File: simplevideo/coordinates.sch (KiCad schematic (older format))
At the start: 3 parts, among them U1 4040, U4 4040, U5 4040

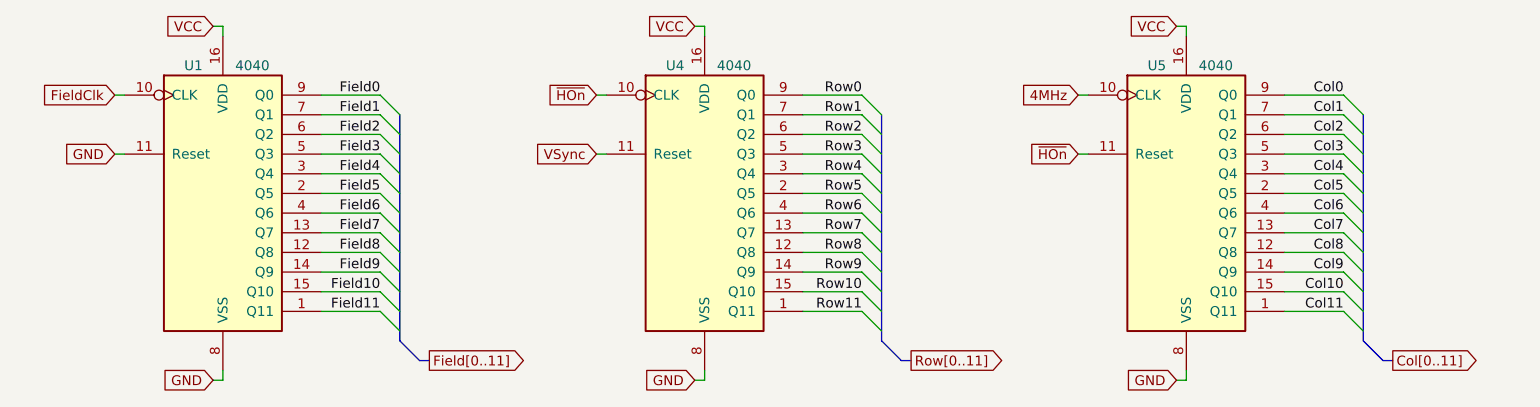
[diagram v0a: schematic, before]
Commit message: Include 6502, ROM, etc in circuit, all laid out together
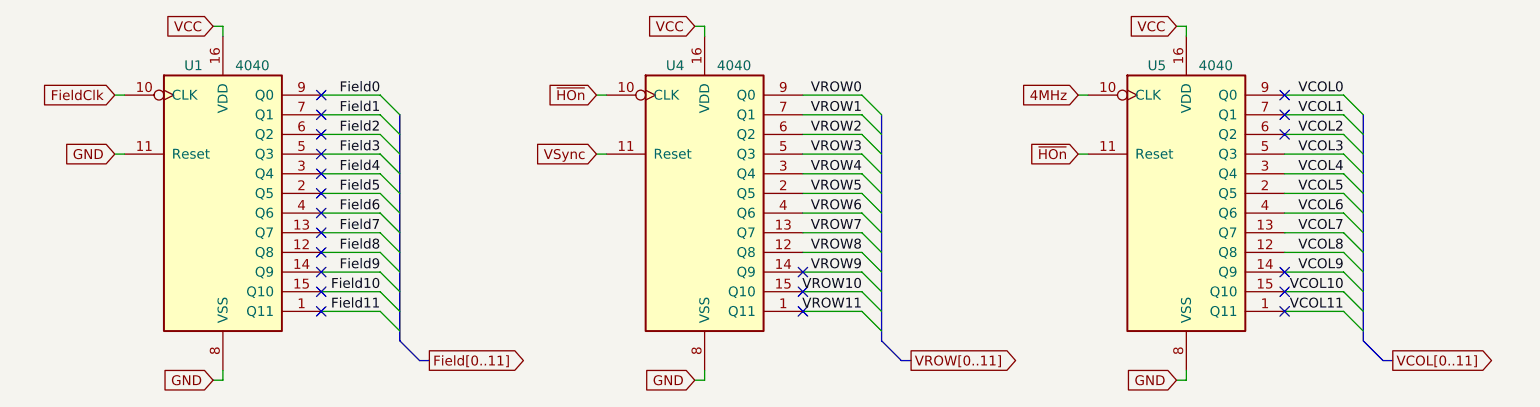
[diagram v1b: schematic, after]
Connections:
- net Col0 renamed VCOL0
- net Col1 renamed VCOL1
- net Col10 renamed VCOL10
- net Col11 renamed VCOL11
- net Col2 renamed VCOL2
- net Col3 renamed VCOL3
- net Col4 renamed VCOL4
- net Col5 renamed VCOL5
- net Col6 renamed VCOL6
- net Col7 renamed VCOL7
- net Col8 renamed VCOL8
- net Col9 renamed VCOL9
- net Row0 renamed VROW0
- net Row1 renamed VROW1
- net Row10 renamed VROW10
- net Row11 renamed VROW11
- net Row2 renamed VROW2
- net Row3 renamed VROW3
- net Row4 renamed VROW4
- net Row5 renamed VROW5
- net Row6 renamed VROW6
- net Row7 renamed VROW7
- net Row8 renamed VROW8
- net Row9 renamed VROW9
- no-connect marks 0 -> 21
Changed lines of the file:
@@
 $Descr A4 11693 8268
 encoding utf-8
-Sheet 5 5
+Sheet 5 7
 Title ""
 Date ""
@@
 	6800 4400 6850 4400
 Text GLabel 6850 4400 2    50   Output ~ 0
-Row[0..11]
+VROW[0..11]
 $Comp
 L 4xxx:4040 U5
@@
 	9250 4400 9300 4400
 Text GLabel 9300 4400 2    50   Output ~ 0
-Col[0..11]
+VCOL[0..11]
 Text Label 4150 3050 2    50   ~ 0
 Field0
@@
 Text Label 4150 4150 2    50   ~ 0
 Field11
-Text Label 6600 3050 2    50   ~ 0
-Row0
-Text Label 6600 3150 2    50   ~ 0
-Row1
-Text Label 6600 3250 2    50   ~ 0
-Row2
-Text Label 6600 3350 2    50   ~ 0
-Row3
-Text Label 6600 3450 2    50   ~ 0
-Row4
-Text Label 6600 3550 2    50   ~ 0
-Row5
-Text Label 6600 3650 2    50   ~ 0
-Row6
-Text Label 6600 3750 2    50   ~ 0
-Row7
-Text Label 6600 3850 2    50   ~ 0
-Row8
-Text Label 6600 3950 2    50   ~ 0
-Row9
-Text Label 6600 4050 2    50   ~ 0
-Row10
-Text Label 6600 4150 2    50   ~ 0
-Row11
-Text Label 9050 3050 2    50   ~ 0
-Col0
-Text Label 9050 3150 2    50   ~ 0
-Col1
-Text Label 9050 3250 2    50   ~ 0
-Col2
-Text Label 9050 3350 2    50   ~ 0
-Col3
-Text Label 9050 3450 2    50   ~ 0
-Col4
-Text Label 9050 3550 2    50   ~ 0
-Col5
-Text Label 9050 3650 2    50   ~ 0
-Col6
-Text Label 9050 3750 2    50   ~ 0
-Col7
-Text Label 9050 3850 2    50   ~ 0
-Col8
-Text Label 9050 3950 2    50   ~ 0
-Col9
-Text Label 9050 4050 2    50   ~ 0
-Col10
-Text Label 9050 4150 2    50   ~ 0
-Col11
 Text GLabel 7700 3050 0    50   Input ~ 0
 4MHz
 Text GLabel 7700 3350 0    50   Input ~ 0
 ~HOn
+Text Label 9050 3050 2    50   ~ 0
+VCOL0
+Text Label 9050 3150 2    50   ~ 0
+VCOL1
+Text Label 9050 3250 2    50   ~ 0
+VCOL2
+Text Label 9050 3350 2    50   ~ 0
+VCOL3
+Text Label 9050 3450 2    50   ~ 0
+VCOL4
+Text Label 9050 3550 2    50   ~ 0
+VCOL5
+Text Label 9050 3650 2    50   ~ 0
+VCOL6
+Text Label 9050 3750 2    50   ~ 0
+VCOL7
+Text Label 9050 3850 2    50   ~ 0
+VCOL8
+Text Label 9050 3950 2    50   ~ 0
+VCOL9
+Text Label 9050 4050 2    50   ~ 0
+VCOL10
+Text Label 9050 4150 2    50   ~ 0
+VCOL11
+Text Label 6600 3050 2    50   ~ 0
+VROW0
+Text Label 6600 3150 2    50   ~ 0
+VROW1
+Text Label 6600 3250 2    50   ~ 0
+VROW2
+Text Label 6600 3350 2    50   ~ 0
+VROW3
+Text Label 6600 3450 2    50   ~ 0
+VROW4
+Text Label 6600 3550 2    50   ~ 0
+VROW5
+Text Label 6600 3650 2    50   ~ 0
+VROW6
+Text Label 6600 3750 2    50   ~ 0
+VROW7
+Text Label 6600 3850 2    50   ~ 0
+VROW8
+Text Label 6600 3950 2    50   ~ 0
+VROW9
+Text Label 6600 4050 2    50   ~ 0
+VROW10
+Text Label 6600 4150 2    50   ~ 0
+VROW11
+NoConn ~ 8750 3950
+NoConn ~ 8750 4050
+NoConn ~ 8750 4150
+NoConn ~ 6300 3950
+NoConn ~ 6300 4050
+NoConn ~ 6300 4150
+NoConn ~ 3850 3050
+NoConn ~ 3850 3150
+NoConn ~ 3850 3250
+NoConn ~ 3850 3350
+NoConn ~ 3850 3450
+NoConn ~ 3850 3550
+NoConn ~ 3850 3650
+NoConn ~ 3850 3750
+NoConn ~ 3850 3850
+NoConn ~ 3850 4050
+NoConn ~ 3850 3950
+NoConn ~ 3850 4150
+NoConn ~ 8750 3150
+NoConn ~ 8750 3050
+NoConn ~ 8750 3250
 Wire Bus Line
 	4250 3150 4250 4300

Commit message: New address decoding scheme and complete breadboard layout, should be ready to build
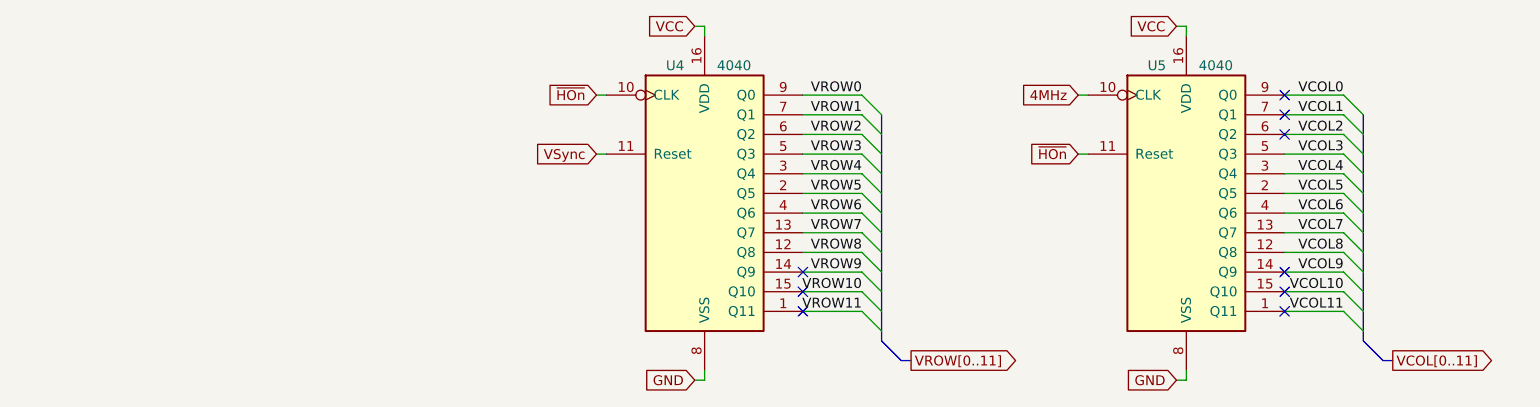
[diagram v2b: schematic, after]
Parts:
- removed U1: 4040, Package_DIP:DIP-16_W7.62mm, symbol 4xxx:4040
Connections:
- no-connect marks 21 -> 9
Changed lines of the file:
@@
 $EndDescr
-$Comp
-L 4xxx:4040 U1
-U 1 1 5EE32031
-P 3350 3550
-F 0 "U1" H 3200 4200 50  0000 C CNN
-F 1 "4040" H 3500 4200 50  0000 C CNN
-F 2 "Package_DIP:DIP-16_W7.62mm" H 3350 3550 50  0001 C CNN
-F 3 "http://www.intersil.com/content/dam/Intersil/documents/cd40/cd4020bms-24bms-40bms.pdf" H 3350 3550 50  0001 C CNN
-	1    3350 3550
-	1    0    0    -1
-$EndComp
-Text GLabel 2800 3050 0    50   Input ~ 0
-FieldClk
-Wire Wire Line
-	2800 3050 2850 3050
-Wire Wire Line
-	2850 3350 2800 3350
-Text GLabel 2800 3350 0    50   Input ~ 0
-GND
-Text GLabel 3300 4500 0    50   Input ~ 0
-GND
-Wire Wire Line
-	3300 4500 3350 4500
-Wire Wire Line
-	3350 4500 3350 4450
-Text GLabel 3300 2700 0    50   Input ~ 0
-VCC
-Wire Wire Line
-	3300 2700 3350 2700
-Wire Wire Line
-	3350 2700 3350 2750
-Wire Wire Line
-	3850 3050 4150 3050
-Wire Wire Line
-	3850 3150 4150 3150
-Wire Wire Line
-	3850 3250 4150 3250
-Wire Wire Line
-	3850 3350 4150 3350
-Wire Wire Line
-	3850 3450 4150 3450
-Wire Wire Line
-	3850 3550 4150 3550
-Wire Wire Line
-	3850 3650 4150 3650
-Wire Wire Line
-	3850 3750 4150 3750
-Wire Wire Line
-	3850 3850 4150 3850
-Wire Wire Line
-	3850 3950 4150 3950
-Wire Wire Line
-	3850 4050 4150 4050
-Wire Wire Line
-	3850 4150 4150 4150
-Entry Wire Line
-	4150 3050 4250 3150
-Entry Wire Line
-	4150 3150 4250 3250
-Entry Wire Line
-	4150 3250 4250 3350
-Entry Wire Line
-	4150 3350 4250 3450
-Entry Wire Line
-	4150 3450 4250 3550
-Entry Wire Line
-	4150 3550 4250 3650
-Entry Wire Line
-	4150 3650 4250 3750
-Entry Wire Line
-	4150 3750 4250 3850
-Entry Wire Line
-	4150 3850 4250 3950
-Entry Wire Line
-	4150 3950 4250 4050
-Entry Wire Line
-	4150 4050 4250 4150
-Entry Wire Line
-	4150 4150 4250 4250
-Entry Bus Bus
-	4250 4300 4350 4400
-Wire Bus Line
-	4350 4400 4400 4400
-Text GLabel 4400 4400 2    50   Output ~ 0
-Field[0..11]
 $Comp
 L 4xxx:4040 U4
@@
 Text GLabel 9300 4400 2    50   Output ~ 0
 VCOL[0..11]
-Text Label 4150 3050 2    50   ~ 0
-Field0
-Text Label 4150 3150 2    50   ~ 0
-Field1
-Text Label 4150 3250 2    50   ~ 0
-Field2
-Text Label 4150 3350 2    50   ~ 0
-Field3
-Text Label 4150 3450 2    50   ~ 0
-Field4
-Text Label 4150 3550 2    50   ~ 0
-Field5
-Text Label 4150 3650 2    50   ~ 0
-Field6
-Text Label 4150 3750 2    50   ~ 0
-Field7
-Text Label 4150 3850 2    50   ~ 0
-Field8
-Text Label 4150 3950 2    50   ~ 0
-Field9
-Text Label 4150 4050 2    50   ~ 0
-Field10
-Text Label 4150 4150 2    50   ~ 0
-Field11
 Text GLabel 7700 3050 0    50   Input ~ 0
 4MHz
@@
 NoConn ~ 6300 4050
 NoConn ~ 6300 4150
-NoConn ~ 3850 3050
-NoConn ~ 3850 3150
-NoConn ~ 3850 3250
-NoConn ~ 3850 3350
-NoConn ~ 3850 3450
-NoConn ~ 3850 3550
-NoConn ~ 3850 3650
-NoConn ~ 3850 3750
-NoConn ~ 3850 3850
-NoConn ~ 3850 4050
-NoConn ~ 3850 3950
-NoConn ~ 3850 4150
 NoConn ~ 8750 3150
 NoConn ~ 8750 3050
 NoConn ~ 8750 3250
 Wire Bus Line
-	4250 3150 4250 4300
-Wire Bus Line
 	6700 3150 6700 4300
